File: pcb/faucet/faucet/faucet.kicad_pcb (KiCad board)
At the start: 2 copper layers, 55.9 x 50.8 mm, 7 parts, among them J1 Conn_01x04_Female, J2 Jack-DC, P1 Conn_WallPlug

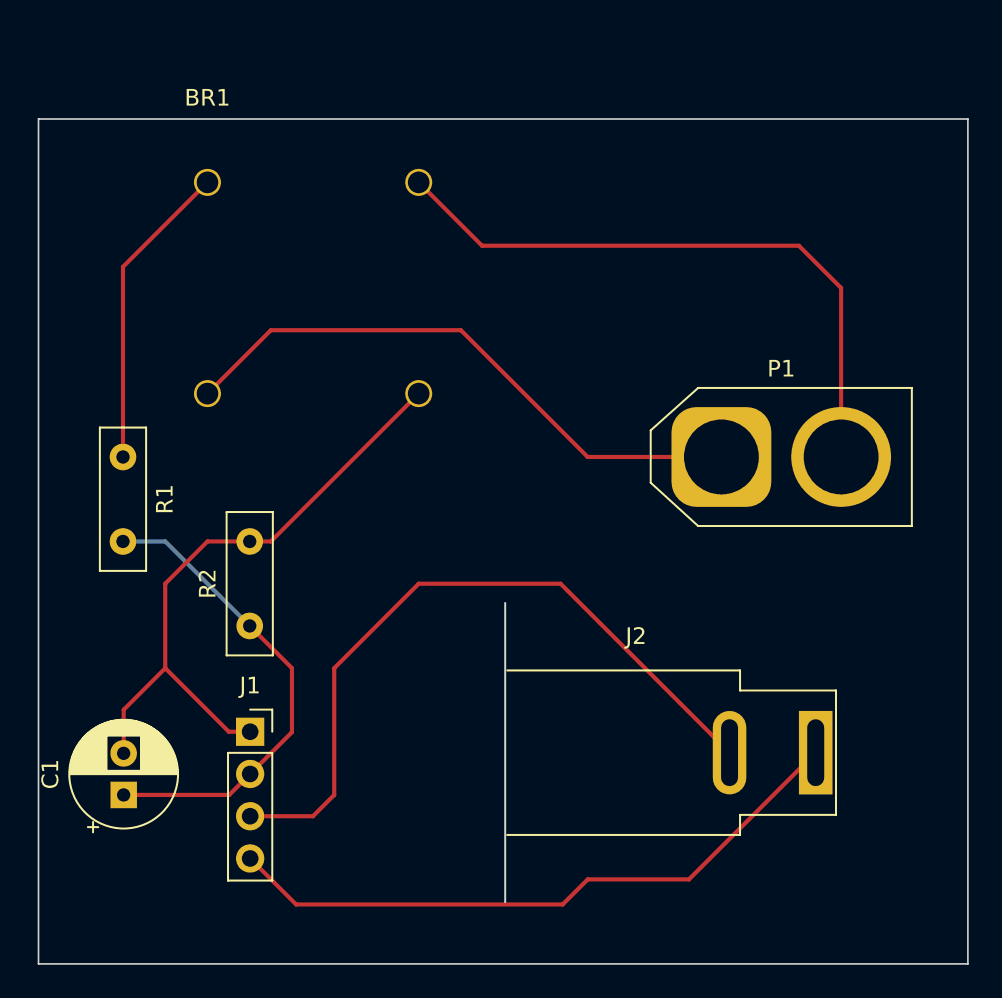
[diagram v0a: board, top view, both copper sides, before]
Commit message: Finalize R and C values, add branding, ordered this board
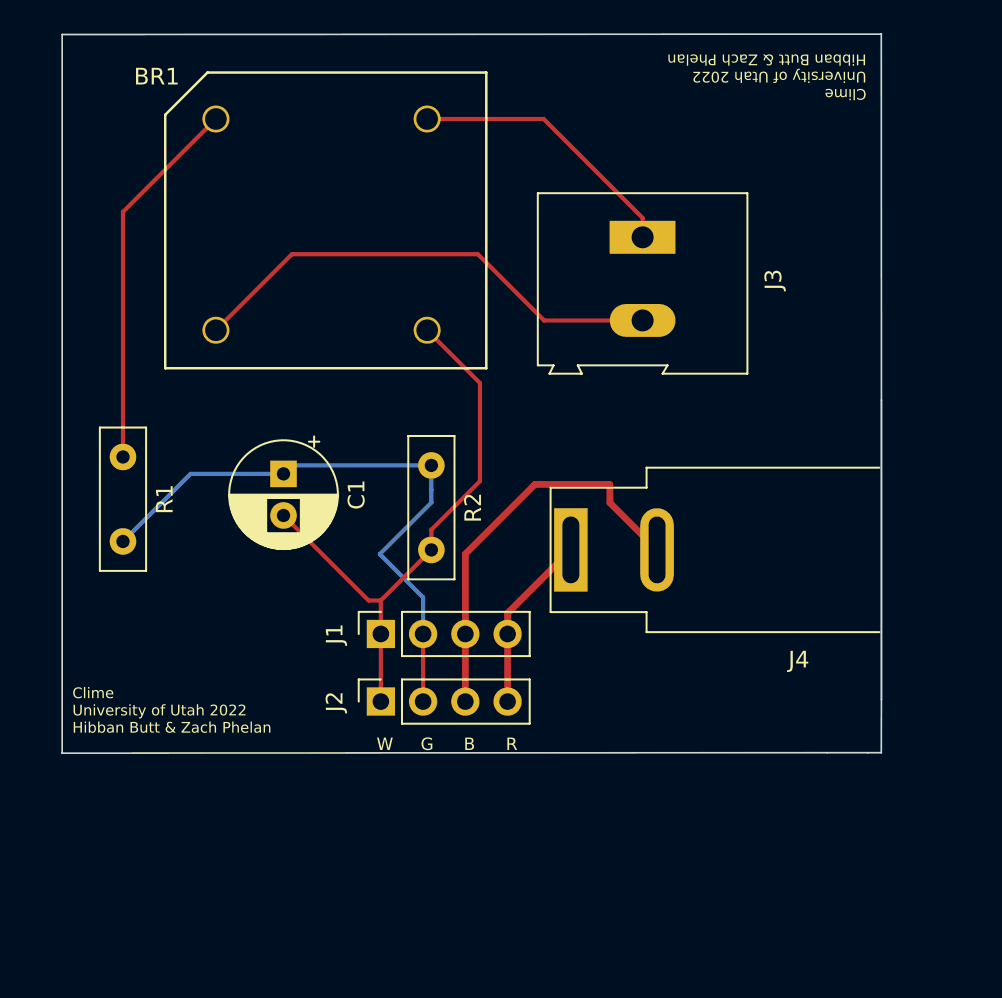
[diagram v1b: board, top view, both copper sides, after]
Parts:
- removed P1: Conn_WallPlug, Connector_AMASS:AMASS_XT60-M_1x02_P7.20mm_Vertical
- added J2: Conn_01x04_Female, Connector_PinSocket_2.54mm:PinSocket_1x04_P2.54mm_Vertical, F.Cu at (117.1, 60.4)
- added J3: Screw_Terminal_01x02, TerminalBlock:TerminalBlock_Altech_AK300-2_P5.00mm, F.Cu at (132.8, 32.5)
- C1: value C -> 220uF
- R1: value 10k -> 51k
- R2: value 1k -> 10k
- moved C1 21.6 mm to (111.3, 46.7), turned to -90 degrees
- moved J4 19.1 mm to (128.5, 51.3), turned to 180 degrees
- moved R2 14.6 mm to (120.1, 46.2), turned to -90 degrees
- moved J1 9.81 mm to (117.1, 56.4), turned to 90 degrees
- moved BR1 3.84 mm to (107.2, 25.4)
- renumbered J2 to J4
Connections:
- net Net-(BR1-Pad4) renamed NEG_SIG
- net Net-(J1-Pad2) renamed POS_SIG
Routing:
- net MTR_PWR: track 38.9 -> 10.7 mm
- net Net-(BR1-Pad2): track 38.2 -> 16.6 mm
- net GND_PWR: track 43.3 -> 24.4 mm
- net POS_SIG: track 28.8 -> 37.0 mm
- net Net-(BR1-Pad3): track 35.6 -> 29.2 mm
- net Net-(BR1-Pad1): track 18.6 -> 22.6 mm
- net NEG_SIG: track 37.9 -> 34.1 mm
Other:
- board size 55.9 x 50.8 mm -> 49.3 x 43.2 mm
- board text added: "B"
- board text added: "Clime University of Utah 2022 Hibban Butt & Zach Phelan"
- board text added: "G"
- board text added: "R"
- board text added: "W"
